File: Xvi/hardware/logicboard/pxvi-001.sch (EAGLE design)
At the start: 70 parts, among them J1 MKR, J4 QWIIC_RIGHT_ANGLE, J5 SPI, J6 QWIIC_RIGHT_ANGLE, J7 DIN5, K1 G5V1, Q1 60V/32A/35mΩ, Q10 60V/32A/35mΩ, Q11 60V/32A/35mΩ, Q12 60V/32A/35mΩ, Q13 60V/32A/35mΩ, Q14 60V/32A/35mΩ, Q15 60V/32A/35mΩ, Q16 60V/32A/35mΩ, Q2 60V/32A/35mΩ, Q3 60V/32A/35mΩ, Q4 60V/32A/35mΩ, Q5 60V/32A/35mΩ, Q6 60V/32A/35mΩ, Q7 60V/32A/35mΩ, Q8 60V/32A/35mΩ, Q9 60V/32A/35mΩ, T1 2SC1815, U1 DS18B20, X1 ADAFRUIT-PCA9685, X2 MKDSN1,5/2-5,08

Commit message: Added THS connector.
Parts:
- added J8: (no value), SparkFun-Connectors:CONN_03JST-PTH
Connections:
- net GND: now also J8.1
- net THS: now also J8.2
- net VCC: now also J8.3
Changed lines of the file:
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@@
 <part name="SUPPLY40" library="supply2" library_urn="urn:adsk.eagle:library:372" deviceset="VCC" device=""/>
 <part name="SUPPLY41" library="supply2" deviceset="GND" device=""/>
+<part name="J8" library="SparkFun-Connectors" library_urn="urn:adsk.eagle:library:513" deviceset="CONN_03" device="JST-PTH" package3d_urn="urn:adsk.eagle:package:38069/1"/>
+<part name="SUPPLY42" library="supply2" library_urn="urn:adsk.eagle:library:372" deviceset="VCC" device=""/>
+<part name="SUPPLY43" library="supply2" deviceset="GND" device=""/>
 </parts>
 <sheets>
@@
 </instance>
 <instance part="SUPPLY41" gate="GND" x="246.38" y="132.08" smashed="yes"/>
+<instance part="J8" gate="J$1" x="190.5" y="182.88" smashed="yes">
+<attribute name="VALUE" x="187.96" y="175.514" size="1.778" layer="96" font="vector"/>
+<attribute name="NAME" x="187.96" y="188.468" size="1.778" layer="95" font="vector"/>
+</instance>
+<instance part="SUPPLY42" gate="G$1" x="205.74" y="190.5" smashed="yes">
+<attribute name="VALUE" x="205.74" y="195.58" size="1.778" layer="96" align="bottom-center"/>
+</instance>
+<instance part="SUPPLY43" gate="GND" x="205.74" y="175.26" smashed="yes"/>
 </instances>
 <busses>
@@
 <pinref part="SUPPLY41" gate="GND" pin="GND"/>
 </segment>
+<segment>
+<pinref part="J8" gate="J$1" pin="1"/>
+<wire x1="198.12" y1="180.34" x2="205.74" y2="180.34" width="0.1524" layer="91"/>
+<wire x1="205.74" y1="180.34" x2="205.74" y2="177.8" width="0.1524" layer="91"/>
+<pinref part="SUPPLY43" gate="GND" pin="GND"/>
+</segment>
 </net>
 <net name="VCC" class="2">
@@
 <pinref part="SUPPLY40" gate="G$1" pin="VCC"/>
 </segment>
+<segment>
+<pinref part="J8" gate="J$1" pin="3"/>
+<wire x1="198.12" y1="185.42" x2="205.74" y2="185.42" width="0.1524" layer="91"/>
+<wire x1="205.74" y1="185.42" x2="205.74" y2="187.96" width="0.1524" layer="91"/>
+<pinref part="SUPPLY42" gate="G$1" pin="VCC"/>
+</segment>
 </net>
 <net name="RST" class="0">
@@
 <label x="347.98" y="50.8" size="0.8128" layer="95" xref="yes"/>
 </segment>
+<segment>
+<pinref part="J8" gate="J$1" pin="2"/>
+<wire x1="198.12" y1="182.88" x2="205.74" y2="182.88" width="0.1524" layer="91"/>
+<label x="205.74" y="182.88" size="0.8128" layer="95" xref="yes"/>
+</segment>
 </net>

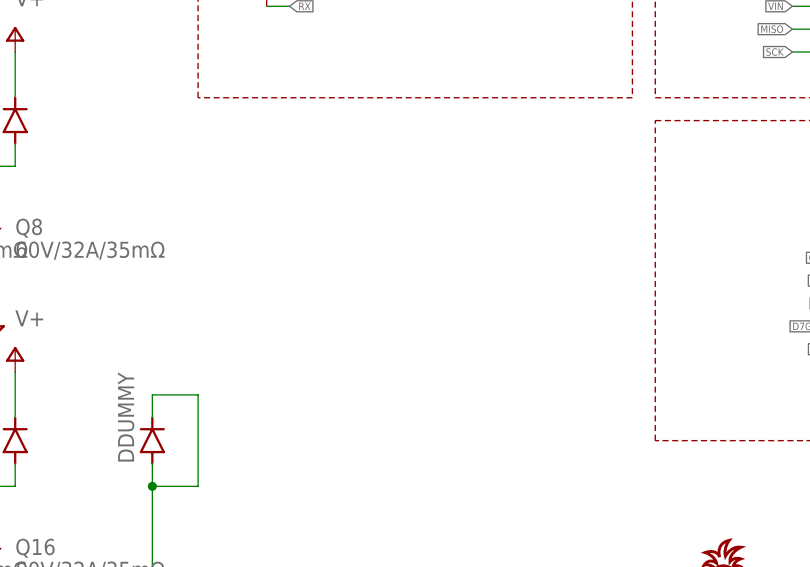
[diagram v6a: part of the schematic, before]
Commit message: RST pin.
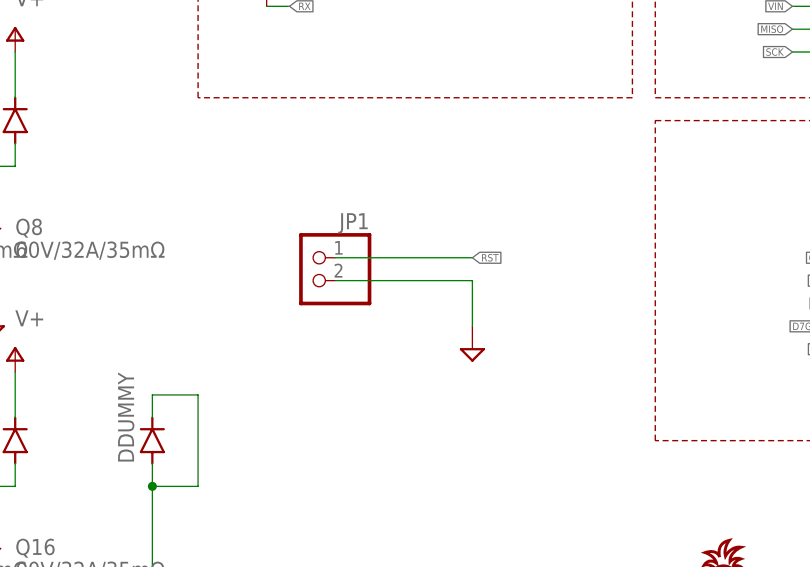
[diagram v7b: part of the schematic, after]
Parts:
- added JP1: (no value), pinhead:PINHD-1X2
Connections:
- net GND: now also JP1.2
- net RST: now also JP1.1
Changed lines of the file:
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@@
 <part name="SUPPLY42" library="supply2" library_urn="urn:adsk.eagle:library:372" deviceset="VCC" device=""/>
 <part name="SUPPLY43" library="supply2" deviceset="GND" device=""/>
+<part name="JP1" library="pinhead" library_urn="urn:adsk.eagle:library:325" deviceset="PINHD-1X2" device="" package3d_urn="urn:adsk.eagle:package:22435/2"/>
+<part name="SUPPLY44" library="supply2" deviceset="GND" device=""/>
 </parts>
 <sheets>
@@
 </instance>
 <instance part="SUPPLY43" gate="GND" x="205.74" y="175.26" smashed="yes"/>
+<instance part="JP1" gate="G$1" x="266.7" y="48.26" smashed="yes" rot="MR0">
+<attribute name="NAME" x="273.05" y="53.975" size="1.778" layer="95" rot="MR0"/>
+<attribute name="VALUE" x="273.05" y="43.18" size="1.778" layer="96" rot="MR0"/>
+</instance>
+<instance part="SUPPLY44" gate="GND" x="284.48" y="40.64" smashed="yes"/>
 </instances>
 <busses>
@@
 <pinref part="SUPPLY43" gate="GND" pin="GND"/>
 </segment>
+<segment>
+<pinref part="JP1" gate="G$1" pin="2"/>
+<wire x1="269.24" y1="48.26" x2="284.48" y2="48.26" width="0.1524" layer="91"/>
+<wire x1="284.48" y1="48.26" x2="284.48" y2="43.18" width="0.1524" layer="91"/>
+<pinref part="SUPPLY44" gate="GND" pin="GND"/>
+</segment>
 </net>
 <net name="VCC" class="2">
@@
 <pinref part="J5" gate="G$1" pin="5"/>
 </segment>
+<segment>
+<pinref part="JP1" gate="G$1" pin="1"/>
+<wire x1="269.24" y1="50.8" x2="284.48" y2="50.8" width="0.1524" layer="91"/>
+<label x="284.48" y="50.8" size="0.8128" layer="95" xref="yes"/>
+</segment>
 </net>

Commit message: Cap and diode.
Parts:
- added C10, C101, C11, C12, C13, C14, C15, C16, C17, C18, C19, C20, C21, C22, C23, C24, C9: (no value), rcl:C-EUC3216
- added R6: (no value), rcl:R-EU_R3216
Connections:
- new net N$3: DDUMMY.A, R6.1
- net GND: now also C24.2; no longer DDUMMY.A
- net LD00: now also C101.2
- net LD01: now also C9.2
- net LD02: now also C10.2
- net LD03: now also C11.2
- net LD04: now also C12.2
- net LD05: now also C13.2
- net LD06: now also C14.2
- net LD07: now also C15.2
- net LD08: now also C16.2
- net LD09: now also C17.2
- net LD10: now also C18.2
- net LD11: now also C19.2
- net LD12: now also C20.2
- net LD13: now also C21.2
- net LD14: now also C22.2
- net LD15: now also C23.2
- net V+: now also C10.1, C101.1, C11.1, C12.1, C13.1, C14.1, C15.1, C16.1, C17.1, C18.1, C19.1, C20.1, C21.1, C22.1, C23.1, C9.1, R6.2
- net VCC: now also C24.1
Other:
- moved on the sheet: C6, C7, C8, DDUMMY
